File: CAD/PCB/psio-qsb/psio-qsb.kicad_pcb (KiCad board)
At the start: 2 copper layers, 55.3 x 18 mm, 2 parts, among them J1 62684-402100ALF, U1 Conn_04x17_PSX_PIO

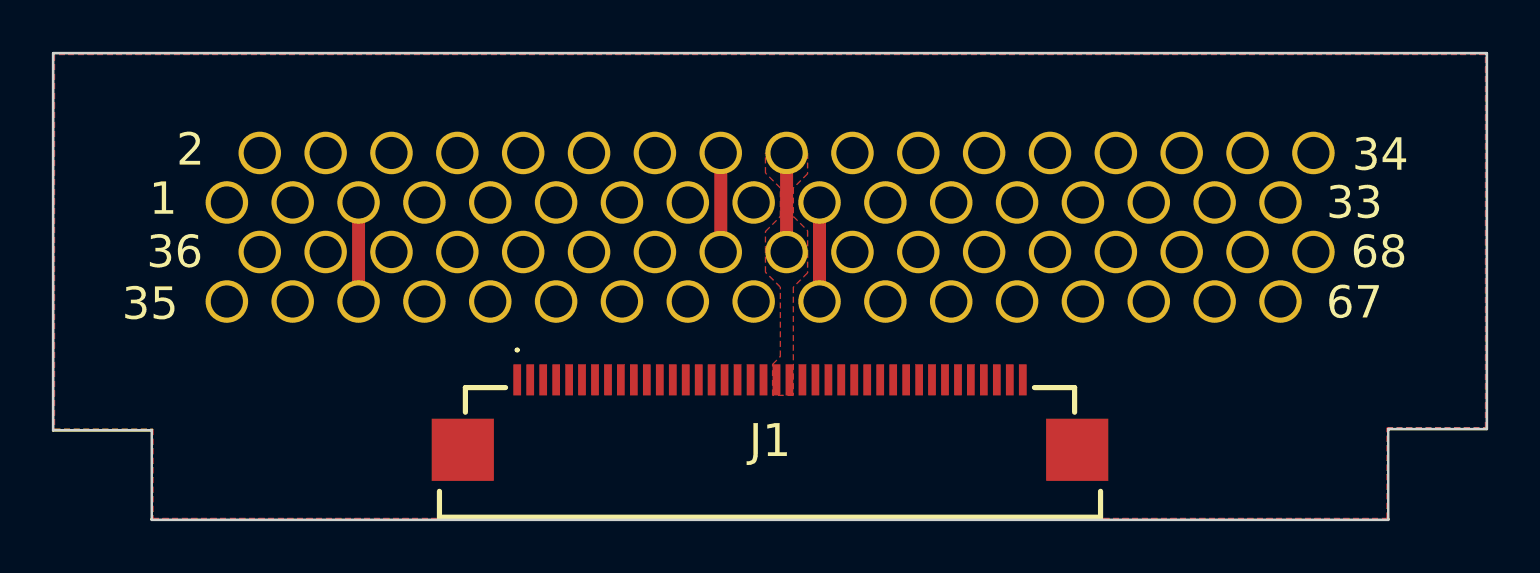
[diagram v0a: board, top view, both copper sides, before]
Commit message: reloc - further routing of psio qsb
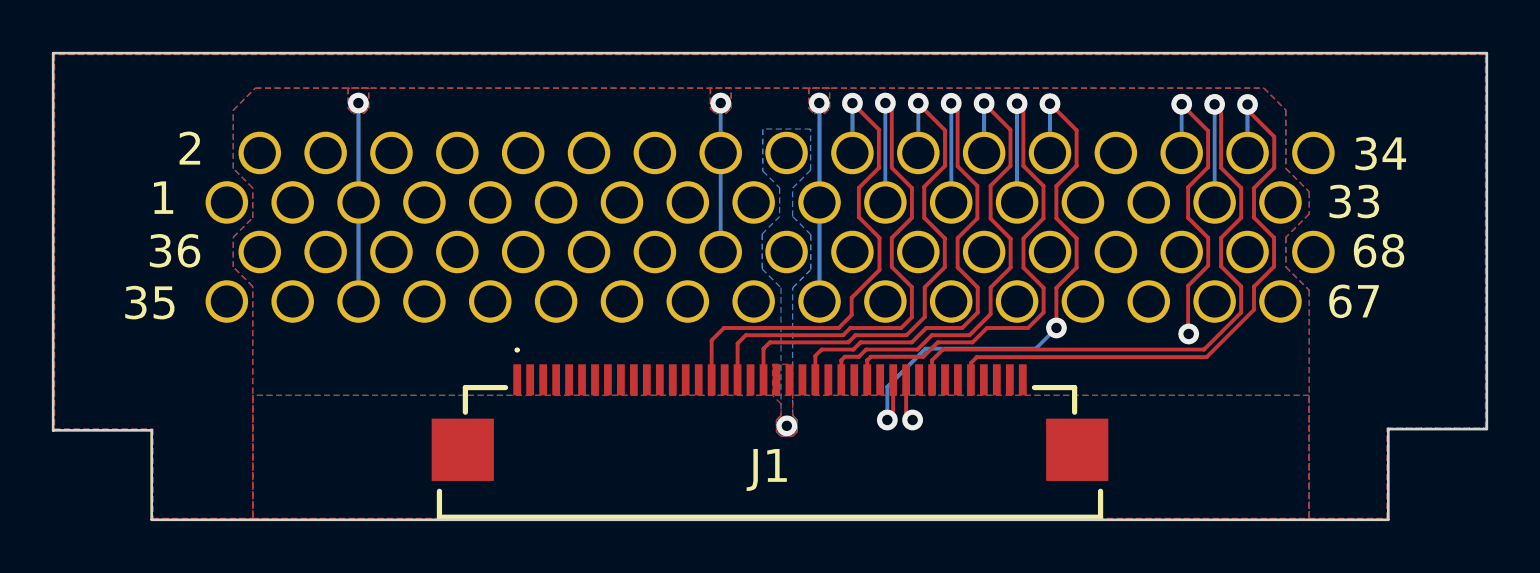
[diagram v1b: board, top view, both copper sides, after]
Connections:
- J1 pad 23: unconnected-(J1-Pad23) -> SA9
- J1 pad 24: unconnected-(J1-Pad24) -> SA10
- J1 pad 25: unconnected-(J1-Pad25) -> SA11
- J1 pad 26: unconnected-(J1-Pad26) -> SA12
- J1 pad 27: unconnected-(J1-Pad27) -> SA13
- J1 pad 28: unconnected-(J1-Pad28) -> SA14
- J1 pad 29: unconnected-(J1-Pad29) -> SA15
- J1 pad 30: unconnected-(J1-Pad30) -> SA16
- J1 pad 31: unconnected-(J1-Pad31) -> SRD
- J1 pad 32: unconnected-(J1-Pad32) -> SWR0
- J1 pad 33: unconnected-(J1-Pad33) -> CS5
- J1 pad 34: unconnected-(J1-Pad34) -> IRQ2
- J1 pad 35: unconnected-(J1-Pad35) -> GND
- J1 pad 36: unconnected-(J1-Pad36) -> SYSCK
- J1 pad 37: unconnected-(J1-Pad37) -> GND
- J1 pad 38: unconnected-(J1-Pad38) -> LRCK
- J1 pad 39: unconnected-(J1-Pad39) -> BCK
- J1 pad 40: unconnected-(J1-Pad40) -> SDAT
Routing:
- net CS5: track 0.00 -> 26.3 mm, vias 0 -> 1
- net SYSCK: track 0.00 -> 23.6 mm, vias 0 -> 1
- net SA16: track 0.00 -> 22.3 mm, vias 0 -> 3
- net SA6: track 0.00 -> 21.7 mm, vias 0 -> 1
- net SA14: track 0.00 -> 21.3 mm, vias 0 -> 1
- net SA10: track 0.00 -> 20.8 mm, vias 0 -> 1
- net SA8: track 0.00 -> 19.5 mm, vias 0 -> 1
- net SA4: track 0.00 -> 18.9 mm, vias 0 -> 1
- net SA12: track 0.00 -> 18.7 mm, vias 0 -> 1
- net SRD: track 0.00 -> 13.8 mm, vias 0 -> 3
- net GND: track 11.5 -> 21.1 mm, vias 0 -> 3
- net +3.5V: track 3.82 -> 0.00 mm, vias 0 -> 1
- added copper zone on B.Cu, net +3.5V

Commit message: reloc - finish routing psio qsb
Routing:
- net GND: track 21.1 -> 0.00 mm, vias 3 -> 58
- net RST: track 0.00 -> 18.8 mm
- net CS0: track 0.00 -> 17.2 mm, vias 0 -> 1
- net SD0: track 0.00 -> 17.1 mm, vias 0 -> 1
- net BCK: track 0.00 -> 16.6 mm, vias 0 -> 1
- net SWR0: track 0.00 -> 15.0 mm, vias 0 -> 1
- net LRCK: track 0.00 -> 14.7 mm, vias 0 -> 1
- net SD2: track 0.00 -> 14.2 mm, vias 0 -> 1
- net SD4: track 0.00 -> 14.2 mm, vias 0 -> 1
- net IRQ10: track 0.00 -> 12.6 mm, vias 0 -> 1
- net SD6: track 0.00 -> 12.1 mm, vias 0 -> 1
- net IRQ2: track 0.00 -> 12.1 mm
- net SDAT: track 0.00 -> 11.8 mm
- net SD1: track 0.00 -> 11.6 mm, vias 0 -> 1
- net CS5: track 26.3 -> 15.3 mm
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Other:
- board text added: "Created by Y2K"
- board text added: "PSXpress PSIO QSB"
- board text removed: "1"
- board text removed: "2"
- board text removed: "33"
- board text removed: "34"
- board text removed: "35"
- board text removed: "36"
- board text removed: "67"
- board text removed: "68"

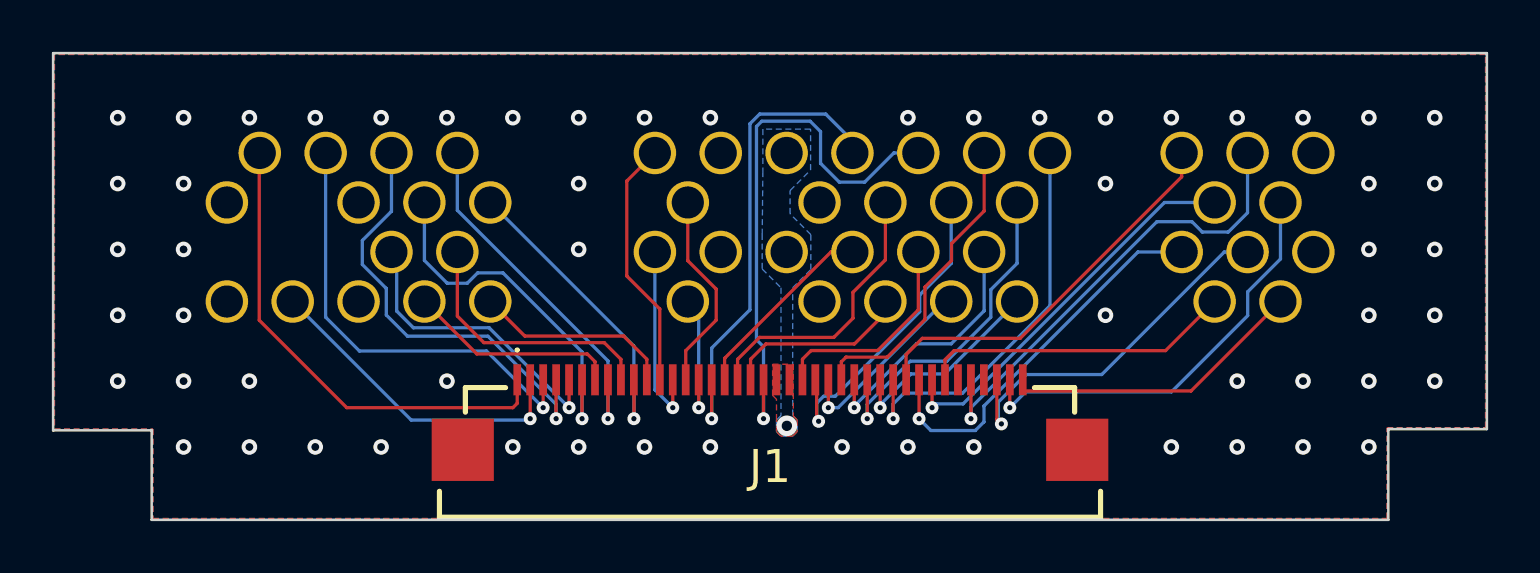
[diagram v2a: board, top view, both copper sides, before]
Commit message: reloc - clean up psio-qsb design
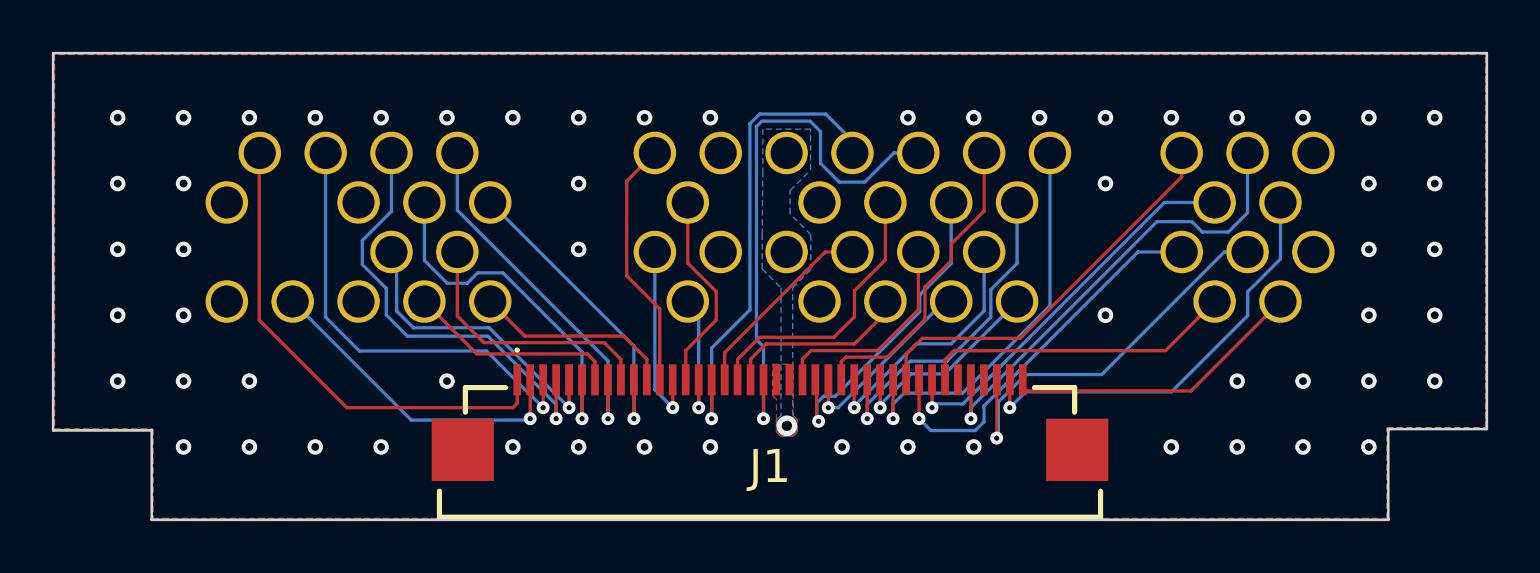
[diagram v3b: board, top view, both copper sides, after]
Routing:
- net LRCK: track 14.7 -> 15.7 mm
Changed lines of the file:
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@@
   (segment (start 143.925 123.1953) (end 143.925 119.535) (width 0.127) (layer "F.Cu") (net 7))
   (segment (start 145.2 127.2) (end 145.2 124.4703) (width 0.127) (layer "F.Cu") (net 7))
-  (segment (start 146.28 122.605) (end 146.28 120.36) (width 0.127) (layer "F.Cu") (net 8))
-  (segment (start 147.375 124.8983) (end 147.375 123.7) (width 0.127) (layer "F.Cu") (net 8))
   (segment (start 146.2 127.2) (end 146.2 126.0733) (width 0.127) (layer "F.Cu") (net 8))
-  (segment (start 147.375 123.7) (end 146.28 122.605) (width 0.127) (layer "F.Cu") (net 8))
+  (segment (start 147.375 124.8983) (end 147.375 123.8) (width 0.127) (layer "F.Cu") (net 8))
   (segment (start 146.2 126.0733) (end 147.375 124.8983) (width 0.127) (layer "F.Cu") (net 8))
+  (segment (start 146.28 122.705) (end 146.28 120.36) (width 0.127) (layer "F.Cu") (net 8))
+  (segment (start 147.375 123.8) (end 146.28 122.705) (width 0.127) (layer "F.Cu") (net 8))
   (via (at 150.1 128.975) (size 0.8) (drill 0.4) (layers "F.Cu" "B.Cu") (net 9))
   (segment (start 147.2 128.7) (end 147.2 127.2) (width 0.127) (layer "F.Cu") (net 10))
@@
   (segment (start 147.2 125.975) (end 147.2 128.7) (width 0.127) (layer "B.Cu") (net 10))
   (segment (start 149.05 116.95) (end 148.675 117.325) (width 0.127) (layer "B.Cu") (net 10))
-  (segment (start 152.65 124.825) (end 152.65 123.825) (width 0.127) (layer "F.Cu") (net 11))
+  (segment (start 153.9 122.575) (end 153.9 120.36) (width 0.127) (layer "F.Cu") (net 11))
+  (segment (start 148.2 127.2) (end 148.2 126.4076) (width 0.127) (layer "F.Cu") (net 11))
+  (segment (start 152.71 123.765) (end 153.9 122.575) (width 0.127) (layer "F.Cu") (net 11))
+  (segment (start 151.912 125.563) (end 152.71 124.765) (width 0.127) (layer "F.Cu") (net 11))
   (segment (start 149.0446 125.563) (end 151.912 125.563) (width 0.127) (layer "F.Cu") (net 11))
-  (segment (start 151.912 125.563) (end 152.65 124.825) (width 0.127) (layer "F.Cu") (net 11))
-  (segment (start 153.9 122.575) (end 153.9 120.36) (width 0.127) (layer "F.Cu") (net 11))
-  (segment (start 152.65 123.825) (end 153.9 122.575) (width 0.127) (layer "F.Cu") (net 11))
-  (segment (start 148.2 127.2) (end 148.2 126.4076) (width 0.127) (layer "F.Cu") (net 11))
   (segment (start 148.2 126.4076) (end 149.0446 125.563) (width 0.127) (layer "F.Cu") (net 11))
+  (segment (start 152.71 124.765) (end 152.71 123.765) (width 0.127) (layer "F.Cu") (net 11))
   (segment (start 149.2 128.7) (end 149.2 127.2) (width 0.127) (layer "F.Cu") (net 12))
   (via (at 149.2 128.7) (size 0.5) (drill 0.2) (layers "F.Cu" "B.Cu") (net 12))
@@
   (segment (start 146.7 124.6) (end 146.28 124.18) (width 0.127) (layer "B.Cu") (net 27))
   (segment (start 146.7 128.275) (end 146.7 124.6) (width 0.127) (layer "B.Cu") (net 27))
-  (segment (start 147.7 126.3697) (end 151.7997 122.27) (width 0.127) (layer "F.Cu") (net 28))
-  (segment (start 151.7997 122.27) (end 152.63 122.27) (width 0.127) (layer "F.Cu") (net 28))
-  (segment (start 147.7 127.2) (end 147.7 126.3697) (width 0.127) (layer "F.Cu") (net 28))
+  (segment (start 147.7 126.15) (end 151.58 122.27) (width 0.127) (layer "F.Cu") (net 28))
+  (segment (start 151.58 122.27) (end 152.63 122.27) (width 0.127) (layer "F.Cu") (net 28))
+  (segment (start 147.7 127.2) (end 147.7 126.15) (width 0.127) (layer "F.Cu") (net 28))
   (segment (start 148.7 126.4076) (end 149.2906 125.817) (width 0.127) (layer "F.Cu") (net 29))
   (segment (start 149.2906 125.817) (end 152.708 125.817) (width 0.127) (layer "F.Cu") (net 29))
@@
   (segment (start 156.2 126.425) (end 156.2 127.2) (width 0.127) (layer "F.Cu") (net 35))
   (segment (start 166.6 124.18) (end 164.705 126.075) (width 0.127) (layer "F.Cu") (net 35))
-  (segment (start 158.375 128.9) (end 158.2 128.725) (width 0.127) (layer "F.Cu") (net 36))
-  (segment (start 158.2 128.725) (end 158.2 127.2) (width 0.127) (layer "F.Cu") (net 36))
-  (via (at 158.375 128.9) (size 0.5) (drill 0.2) (layers "F.Cu" "B.Cu") (net 36))
-  (segment (start 158.375 128.9) (end 158.2595 128.7845) (width 0.127) (layer "B.Cu") (net 36))
+  (segment (start 158.193982 129.45) (end 158.2 129.443982) (width 0.127) (layer "F.Cu") (net 36))
+  (segment (start 158.2 129.443982) (end 158.2 127.2) (width 0.127) (layer "F.Cu") (net 36))
+  (via (at 158.193982 129.45) (size 0.5) (drill 0.2) (layers "F.Cu" "B.Cu") (net 36))
+  (segment (start 158.193982 129.45) (end 158.2595 129.384482) (width 0.127) (layer "B.Cu") (net 36))
   (segment (start 158.2595 128.0546) (end 159.3174 126.9967) (width 0.127) (layer "B.Cu") (net 36))
+  (segment (start 162.2457 126.9967) (end 166.9724 122.27) (width 0.127) (layer "B.Cu") (net 36))
+  (segment (start 166.9724 122.27) (end 167.87 122.27) (width 0.127) (layer "B.Cu") (net 36))
+  (segment (start 158.2595 129.384482) (end 158.2595 128.0546) (width 0.127) (layer "B.Cu") (net 36))
   (segment (start 159.3174 126.9967) (end 162.2457 126.9967) (width 0.127) (layer "B.Cu") (net 36))
-  (segment (start 166.9724 122.27) (end 167.87 122.27) (width 0.127) (layer "B.Cu") (net 36))
-  (segment (start 158.2595 128.7845) (end 158.2595 128.0546) (width 0.127) (layer "B.Cu") (net 36))
-  (segment (start 162.2457 126.9967) (end 166.9724 122.27) (width 0.127) (layer "B.Cu") (net 36))
   (segment (start 165.6902 127.6298) (end 169.14 124.18) (width 0.127) (layer "F.Cu") (net 37))
   (segment (start 159.2 127.6298) (end 165.6902 127.6298) (width 0.127) (layer "F.Cu") (net 37))
@@
   (segment (start 133.125 128.275) (end 139.5323 128.275) (width 0.127) (layer "F.Cu") (net 38))
   (segment (start 129.77 118.45) (end 129.75 118.47) (width 0.127) (layer "F.Cu") (net 38))
+  (zone (net 0) (net_name "") (layer "F.Cu") (hatch edge 0.5)
+    (connect_pads (clearance 0))
+    (min_thickness 0.25) (filled_areas_thickness no)
+    (keepout (tracks allowed) (vias allowed) (pads allowed) (copperpour not_allowed) (footprints allowed))
+    (fill (thermal_gap 0.5) (thermal_bridge_width 0.5))
+    (polygon
+      (pts
+        (xy 147.64 124.89)
+        (xy 147.64 125.25)
+        (xy 147.56 125.25)
+        (xy 147.56 124.89)
+      )
+    )
+  )
+  (zone (net 0) (net_name "") (layer "F.Cu") (hatch edge 0.5)
+    (connect_pads (clearance 0))
+    (min_thickness 0.25) (filled_areas_thickness no)
+    (keepout (tracks allowed) (vias allowed) (pads allowed) (copperpour not_allowed) (footprints allowed))
+    (fill (thermal_gap 0.5) (thermal_bridge_width 0.5))
+    (polygon
+      (pts
+        (xy 139.35 126.6)
+        (xy 139.35 125.25)
+        (xy 159.55 125.25)
+        (xy 159.55 126.6)
+      )
+    )
+  )
   (zone (net 9) (net_name "+3.5V") (layer "F.Cu") (hatch edge 0.5)
     (priority 6)

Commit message: reloc - finish flex schematic and add finishing touches to psio qsb
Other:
- board text added: "The PSXpress project and it's contributors are not affiliated, associated, authorized, endorsed by, or in any way officially connected with Cybdyn Systems and/or it's proprietors. All product and company names are trademarks or registered trademarks of their respective holders. Use of them does not imply any affiliation with or endorsement by them."
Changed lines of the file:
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@@
     )
+  )
+  (gr_text "The PSXpress project and it's contributors are not affiliated, \nassociated, authorized, endorsed by, or in any way officially \nconnected with Cybdyn Systems and/or it's proprietors. All product \nand company names are trademarks or registered trademarks of \ntheir respective holders. Use of them does not imply any \naffiliation with or endorsement by them." (at 172.675 132.1) (layer "B.SilkS")
+    (effects (font (size 0.5 0.5) (thickness 0.125) bold) (justify left bottom mirror))
   )
   (gr_text "PSXpress PSIO QSB" (at 122.45 116.35) (layer "F.Mask")
